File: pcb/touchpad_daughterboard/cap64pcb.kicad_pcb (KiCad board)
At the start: 2 copper layers, 91.6 x 12 mm, 31 parts, among them J1 SM04B_SURS_TF, Q1 BSS138, Q2 BSS138, U1 MPR121QR2, U2 SPX3819-3.3

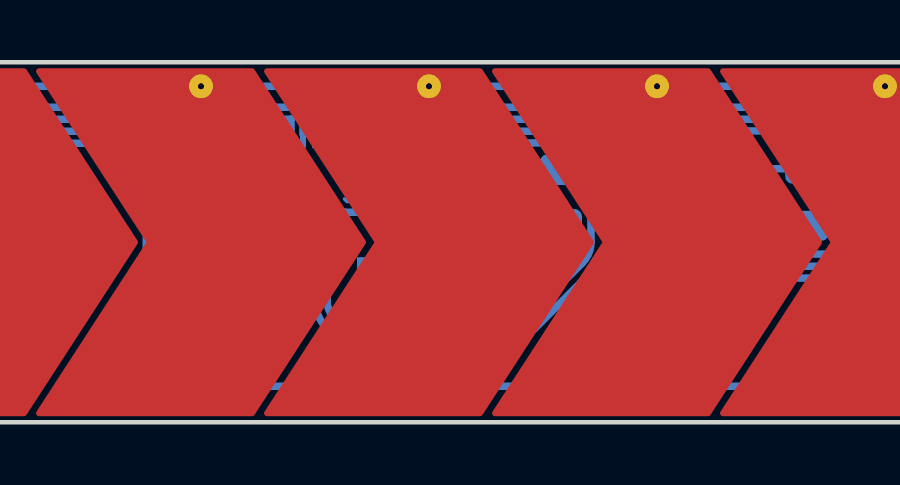
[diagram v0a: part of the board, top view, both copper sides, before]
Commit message: 0603 LED footprint
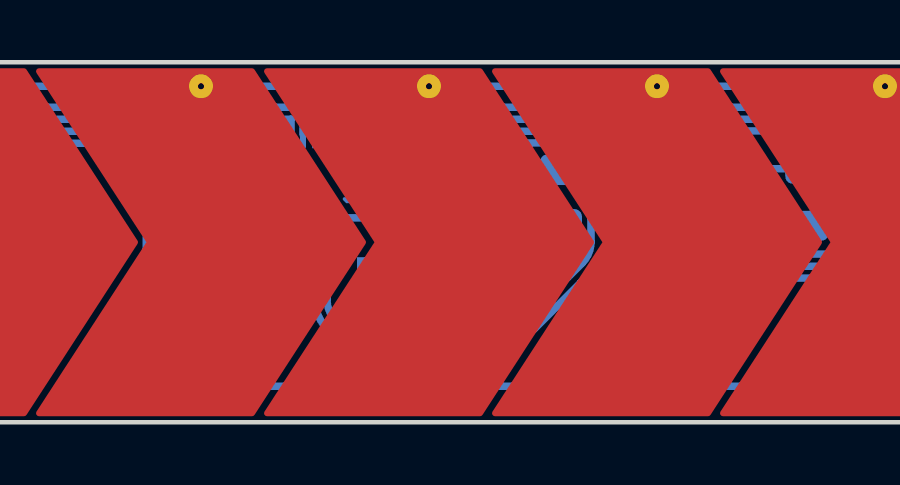
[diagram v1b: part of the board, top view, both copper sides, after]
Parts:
- D1: footprint LED_SMD:LED_0805_2012Metric -> LED_SMD:LED_0603_1608Metric
- moved D1 0.61 mm to (85.4, 44.2)
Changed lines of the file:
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@@
   (net 21 "Net-(TP12-Pad1)")
   (net 22 "Net-(U1-Pad1)")
-  (net 23 "Net-(D1-Pad2)")
-  (net 24 "Net-(J1-Pad4)")
-  (net 25 "Net-(U1-Pad4)")
+  (net 23 "Net-(J1-Pad4)")
+  (net 24 "Net-(JP1-Pad2)")
+  (net 25 "Net-(R4-Pad2)")
   (footprint "cap_pads:CAPPADS_7.6x11.6_Chevron_1" (layer "F.Cu")
     (at 38.2 45)
@@
       (net 7 "SDA") (pinfunction "SDA") (pintype "bidirectional"))
     (pad "4" smd roundrect (at -1.3875 -0.4 90) (size 0.925 0.2) (layers "B.Cu" "B.Paste" "B.Mask") (roundrect_rratio 0.25)
-      (net 25 "Net-(U1-Pad4)") (pinfunction "ADDR") (pintype "input"))
+      (net 24 "Net-(JP1-Pad2)") (pinfunction "ADDR") (pintype "input"))
     (pad "5" smd custom (at -1.3875 -0.8 90) (size 0.115147 0.115147) (layers "B.Cu" "B.Paste" "B.Mask")
       (net 5 "Net-(C5-Pad1)") (pinfunction "VREG") (pintype "passive")
@@
       ))
     (pad "2" smd rect (at 0 0) (size 2 1.5) (layers "B.Cu" "B.Mask")
-      (net 25 "Net-(U1-Pad4)") (pinfunction "C") (pintype "passive"))
+      (net 24 "Net-(JP1-Pad2)") (pinfunction "C") (pintype "passive"))
     (pad "3" smd custom (at 1.8 0) (size 1 0.5) (layers "B.Cu" "B.Mask")
       (net 7 "SDA") (pinfunction "B") (pintype "passive") (zone_connect 2)
@@
       (net 4 "+3V3") (pintype "passive"))
     (pad "2" smd roundrect (at 0.9125 0 270) (size 1.025 1.4) (layers "B.Cu" "B.Paste" "B.Mask") (roundrect_rratio 0.243902)
-      (net 23 "Net-(D1-Pad2)") (pintype "passive"))
+      (net 25 "Net-(R4-Pad2)") (pintype "passive"))
     (model "${KICAD6_3DMODEL_DIR}/Resistor_SMD.3dshapes/R_0805_2012Metric.wrl"
       (offset (xyz 0 0 0))
@@
       (net 8 "SCL") (pinfunction "S") (pintype "passive"))
     (pad "3" smd roundrect (at 0.9375 0) (size 1.475 0.6) (layers "B.Cu" "B.Paste" "B.Mask") (roundrect_rratio 0.25)
-      (net 24 "Net-(J1-Pad4)") (pinfunction "D") (pintype "passive"))
+      (net 23 "Net-(J1-Pad4)") (pinfunction "D") (pintype "passive"))
     (model "${KICAD6_3DMODEL_DIR}/Package_TO_SOT_SMD.3dshapes/SOT-23.wrl"
       (offset (xyz 0 0 0))
@@
     )
   )
-  (footprint "LED_SMD:LED_0805_2012Metric" (layer "B.Cu")
-    (at 85.4 43.594277)
-    (descr "LED SMD 0805 (2012 Metric), square (rectangular) end terminal, IPC_7351 nominal, (Body size source: https://docs.google.com/spreadsheets/d/1BsfQQcO9C6DZCsRaXUlFlo91Tg2WpOkGARC1WS5S8t0/edit?usp=sharing), generated with kicad-footprint-generator")
+  (footprint "LED_SMD:LED_0603_1608Metric" (layer "B.Cu")
+    (at 85.4 44.2)
+    (descr "LED SMD 0603 (1608 Metric), square (rectangular) end terminal, IPC_7351 nominal, (Body size source: http://www.tortai-tech.com/upload/download/2011102023233369053.pdf), generated with kicad-footprint-generator")
     (tags "LED")
     (property "Sheetfile" "cap64pcb.kicad_sch")
     (property "Sheetname" "")
     (attr smd)
-    (fp_text reference "D1" (at 0 1.65) (layer "B.Fab")
-      (effects (font (size 1 1) (thickness 0.15)) (justify mirror))
-    )
-    (fp_text value "INT" (at 0 -1.8) (layer "B.SilkS")
+    (fp_text reference "D1" (at 0 1.43 180) (layer "B.SilkS") hide
+      (effects (font (size 1 1) (thickness 0.15)) (justify mirror))
+    )
+    (fp_text value "INT" (at 0 -1.7 180) (layer "B.SilkS")
       (effects (font (size 1.2 1.2) (thickness 0.3)) (justify mirror))
     )
-    (fp_text user "${REFERENCE}" (at 0 0) (layer "B.Fab")
-      (effects (font (size 0.5 0.5) (thickness 0.08)) (justify mirror))
-    )
-    (fp_line (start -1.685 -0.96) (end 1 -0.96) (layer "B.SilkS") (width 0.12))
-    (fp_line (start -1.685 0.96) (end -1.685 -0.96) (layer "B.SilkS") (width 0.12))
-    (fp_line (start 1 0.96) (end -1.685 0.96) (layer "B.SilkS") (width 0.12))
-    (fp_line (start -1.68 0.95) (end 1.68 0.95) (layer "B.CrtYd") (width 0.05))
-    (fp_line (start 1.68 -0.95) (end -1.68 -0.95) (layer "B.CrtYd") (width 0.05))
-    (fp_line (start -1.68 -0.95) (end -1.68 0.95) (layer "B.CrtYd") (width 0.05))
-    (fp_line (start 1.68 0.95) (end 1.68 -0.95) (layer "B.CrtYd") (width 0.05))
-    (fp_line (start 1 0.6) (end -0.7 0.6) (layer "B.Fab") (width 0.1))
-    (fp_line (start -1 0.3) (end -1 -0.6) (layer "B.Fab") (width 0.1))
-    (fp_line (start 1 -0.6) (end 1 0.6) (layer "B.Fab") (width 0.1))
-    (fp_line (start -0.7 0.6) (end -1 0.3) (layer "B.Fab") (width 0.1))
-    (fp_line (start -1 -0.6) (end 1 -0.6) (layer "B.Fab") (width 0.1))
-    (pad "1" smd roundrect (at -0.9375 0) (size 0.975 1.4) (layers "B.Cu" "B.Paste" "B.Mask") (roundrect_rratio 0.25)
+    (fp_text user "${REFERENCE}" (at 0 0 180) (layer "B.Fab")
+      (effects (font (size 0.4 0.4) (thickness 0.06)) (justify mirror))
+    )
+    (fp_line (start 0.8 0.735) (end -1.485 0.735) (layer "B.SilkS") (width 0.12))
+    (fp_line (start -1.485 0.735) (end -1.485 -0.735) (layer "B.SilkS") (width 0.12))
+    (fp_line (start -1.485 -0.735) (end 0.8 -0.735) (layer "B.SilkS") (width 0.12))
+    (fp_line (start 1.48 -0.73) (end -1.48 -0.73) (layer "B.CrtYd") (width 0.05))
+    (fp_line (start -1.48 0.73) (end 1.48 0.73) (layer "B.CrtYd") (width 0.05))
+    (fp_line (start 1.48 0.73) (end 1.48 -0.73) (layer "B.CrtYd") (width 0.05))
+    (fp_line (start -1.48 -0.73) (end -1.48 0.73) (layer "B.CrtYd") (width 0.05))
+    (fp_line (start 0.8 0.4) (end -0.5 0.4) (layer "B.Fab") (width 0.1))
+    (fp_line (start -0.8 0.1) (end -0.8 -0.4) (layer "B.Fab") (width 0.1))
+    (fp_line (start -0.8 -0.4) (end 0.8 -0.4) (layer "B.Fab") (width 0.1))
+    (fp_line (start -0.5 0.4) (end -0.8 0.1) (layer "B.Fab") (width 0.1))
+    (fp_line (start 0.8 -0.4) (end 0.8 0.4) (layer "B.Fab") (width 0.1))
+    (pad "1" smd roundrect (at -0.7875 0) (size 0.875 0.95) (layers "B.Cu" "B.Paste" "B.Mask") (roundrect_rratio 0.25)
       (net 22 "Net-(U1-Pad1)") (pinfunction "K") (pintype "passive"))
-    (pad "2" smd roundrect (at 0.9375 0) (size 0.975 1.4) (layers "B.Cu" "B.Paste" "B.Mask") (roundrect_rratio 0.25)
-      (net 23 "Net-(D1-Pad2)") (pinfunction "A") (pintype "passive"))
-    (model "${KICAD6_3DMODEL_DIR}/LED_SMD.3dshapes/LED_0805_2012Metric.wrl"
+    (pad "2" smd roundrect (at 0.7875 0) (size 0.875 0.95) (layers "B.Cu" "B.Paste" "B.Mask") (roundrect_rratio 0.25)
+      (net 25 "Net-(R4-Pad2)") (pinfunction "A") (pintype "passive"))
+    (model "${KICAD6_3DMODEL_DIR}/LED_SMD.3dshapes/LED_0603_1608Metric.wrl"
       (offset (xyz 0 0 0))
       (scale (xyz 1 1 1))
@@
       (net 6 "Net-(J1-Pad3)") (pinfunction "Pin_3") (pintype "passive"))
     (pad "4" smd roundrect (at 1.2 1.15 180) (size 0.5 1) (layers "B.Cu" "B.Paste" "B.Mask") (roundrect_rratio 0.25)
-      (net 24 "Net-(J1-Pad4)") (pinfunction "Pin_4") (pintype "passive"))
+      (net 23 "Net-(J1-Pad4)") (pinfunction "Pin_4") (pintype "passive"))
     (pad "MP" smd roundrect (at 2.5 -0.8 180) (size 1.2 1.7) (layers "B.Cu" "B.Paste" "B.Mask") (roundrect_rratio 0.208333)
       (net 2 "GND") (pinfunction "MP") (pintype "power_in"))
@@
   (segment (start 107.475432 40.5) (end 107.085912 40.88952) (width 0.25) (layer "B.Cu") (net 21))
   (segment (start 107.085912 40.88952) (end 100.11048 40.88952) (width 0.25) (layer "B.Cu") (net 21))
-  (segment (start 80.9875 44) (end 80.8 44.1875) (width 0.25) (layer "B.Cu") (net 22))
-  (segment (start 84.4625 44) (end 80.9875 44) (width 0.25) (layer "B.Cu") (net 22))
-  (segment (start 87.680393 43.88717) (end 88.2 44.406777) (width 0.25) (layer "B.Cu") (net 23))
-  (segment (start 86.3375 43.594277) (end 86.973286 43.594277) (width 0.25) (layer "B.Cu") (net 23))
-  (arc (start 87.680393 43.88717) (mid 87.35597 43.670397) (end 86.973286 43.594277) (width 0.25) (layer "B.Cu") (net 23))
-  (segment (start 108.2 42.15) (end 108.2 45.394277) (width 0.25) (layer "B.Cu") (net 24))
-  (segment (start 106.2 47.394277) (end 105.137501 47.394277) (width 0.25) (layer "B.Cu") (net 24))
-  (arc (start 108.2 45.394277) (mid 107.614214 46.808491) (end 106.2 47.394277) (width 0.25) (layer "B.Cu") (net 24))
-  (segment (start 79.6 44.1875) (end 79.6 45) (width 0.25) (layer "B.Cu") (net 25))
-  (segment (start 79.6 45) (end 77.2 47.4) (width 0.25) (layer "B.Cu") (net 25))
+  (segment (start 80.8 44.1875) (end 84.6 44.1875) (width 0.25) (layer "B.Cu") (net 22))
+  (segment (start 84.6 44.1875) (end 84.6125 44.2) (width 0.25) (layer "B.Cu") (net 22))
+  (segment (start 108.2 42.15) (end 108.2 45.394277) (width 0.25) (layer "B.Cu") (net 23))
+  (segment (start 106.2 47.394277) (end 105.137501 47.394277) (width 0.25) (layer "B.Cu") (net 23))
+  (arc (start 108.2 45.394277) (mid 107.614214 46.808491) (end 106.2 47.394277) (width 0.25) (layer "B.Cu") (net 23))
+  (segment (start 79.6 44.1875) (end 79.6 45) (width 0.25) (layer "B.Cu") (net 24))
+  (segment (start 79.6 45) (end 77.2 47.4) (width 0.25) (layer "B.Cu") (net 24))
+  (segment (start 86.394277 44.406777) (end 86.1875 44.2) (width 0.25) (layer "B.Cu") (net 25))
+  (segment (start 88.2 44.406777) (end 86.394277 44.406777) (width 0.25) (layer "B.Cu") (net 25))
   (zone (net 2) (net_name "GND") (layer "B.Cu") (name "back fill") (hatch edge 0.508)
     (connect_pads no (clearance 0.254))

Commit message: simpler JST value silk
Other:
- board text added: "JST- SURS"
- board text removed: "SM04B- SURS-TF"
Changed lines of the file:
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@@
     (effects (font (size 1 1) (thickness 0.2)) (justify mirror))
   )
-  (gr_text "SM04B-\nSURS-TF" (at 121.6 43.4) (layer "B.SilkS")
+  (gr_text "JST-\nSURS" (at 118.26875 43.4) (layer "B.SilkS")
     (effects (font (size 1.2 1.2) (thickness 0.3)) (justify left mirror))
   )
